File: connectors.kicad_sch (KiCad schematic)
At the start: 11 parts, among them J4 USB_C_pycubed, J5 1985807, J6 35362-0650, J7 1985807, J8 1985807, J9 1985807

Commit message: schematic update
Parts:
- removed C32: 4.7uF, Capacitor_SMD:C_0603_1608Metric, symbol Device:C_Small
- removed C33: 0.1uF, Capacitor_SMD:C_0603_1608Metric, symbol Device:C_Small
- removed C34: 22uF, Capacitor_SMD:C_0603_1608Metric, symbol Device:C_Small
- removed J4: USB_C_pycubed, mainboard:USB_C_Receptacle_XKB_U262-161N-4BVC11, symbol mainboard:USB_C_pycubed
- removed J5, J7, J8, J9: 1985807, mainboard:SCREWTERMINAL-3.5MM-2_LOCK, symbol mainboard:M023.5MM_LOCK
- removed J6: 35362-0650, mainboard:MOLEX_35362-0650, symbol mainboard:35362-0650
- removed R39, R40: 5.1k, Resistor_SMD:R_0603_1608Metric, symbol Device:R_US
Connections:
- no-connect marks 2 -> 0
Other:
- note removed: "(Screw Terminals)"
- note removed: "Battery Board"
- note removed: "Battery Connection"
- note removed: "High Side Switches (Screw Terminals)"
- note removed: "Low Side Switch"
- note removed: "Power Connectors: USB-C Power Delivery to 2S Li-ion Battery"

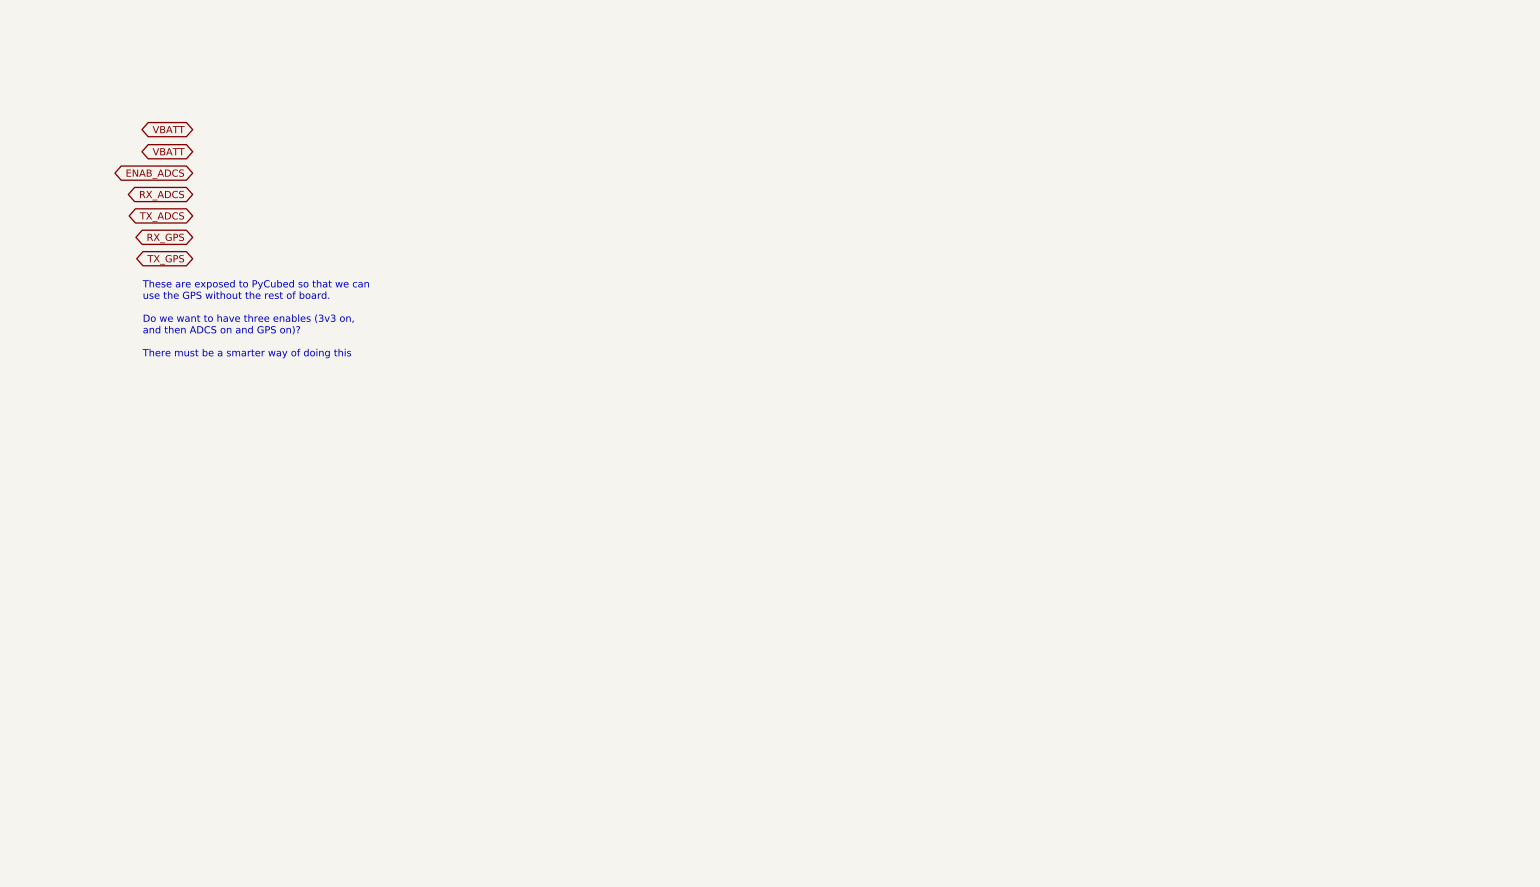
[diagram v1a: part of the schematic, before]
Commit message: update schematic
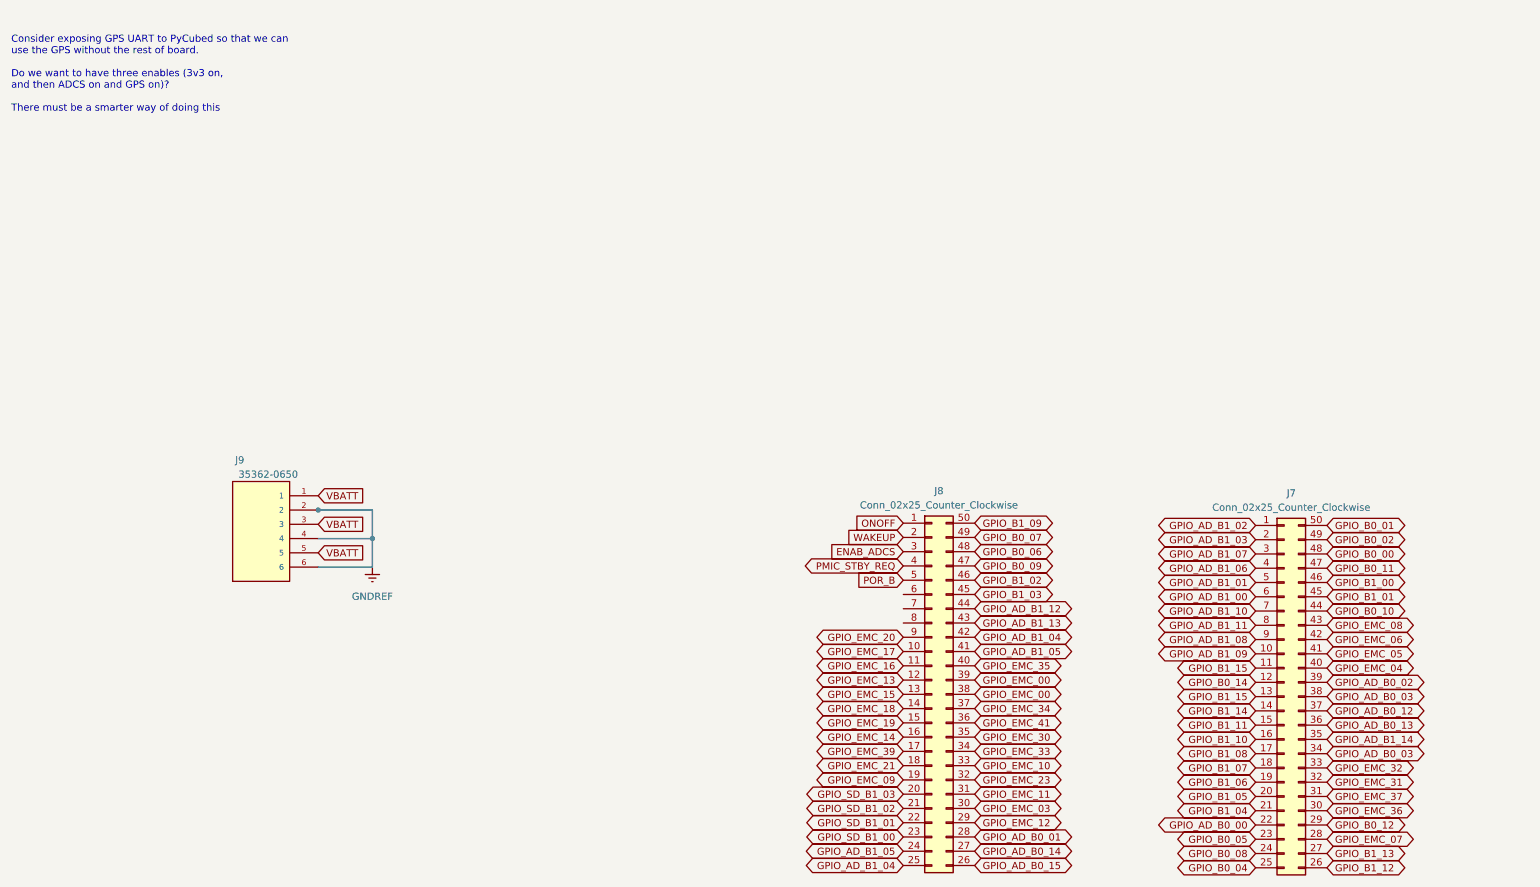
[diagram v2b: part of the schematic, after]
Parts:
- added J7, J8: Conn_02x25_Counter_Clockwise, symbol Connector_Generic:Conn_02x25_Counter_Clockwise
- added J9: 35362-0650, mainboard:MOLEX_35362-0650, symbol mainboard:35362-0650
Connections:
- net ENAB_ADCS: now also J8.3 (Pin_3)
- net VBATT: now also J9.1, J9.3, J9.5
- new net: J9.2, J9.4, J9.6
- new net GPIO_AD_B0_00: J7.22 (Pin_22)
- new net GPIO_AD_B0_01: J8.28 (Pin_28)
- new net GPIO_AD_B0_02: J7.39 (Pin_39)
- new net GPIO_AD_B0_03: J7.34 (Pin_34), J7.38 (Pin_38)
- new net GPIO_AD_B0_12: J7.37 (Pin_37)
- new net GPIO_AD_B0_13: J7.36 (Pin_36)
- new net GPIO_AD_B0_14: J8.27 (Pin_27)
- new net GPIO_AD_B0_15: J8.26 (Pin_26)
- new net GPIO_AD_B1_00: J7.6 (Pin_6)
- new net GPIO_AD_B1_01: J7.5 (Pin_5)
- new net GPIO_AD_B1_02: J7.1 (Pin_1)
- new net GPIO_AD_B1_03: J7.2 (Pin_2)
- new net GPIO_AD_B1_04: J8.25 (Pin_25), J8.42 (Pin_42)
- new net GPIO_AD_B1_05: J8.24 (Pin_24), J8.41 (Pin_41)
- new net GPIO_AD_B1_06: J7.4 (Pin_4)
- new net GPIO_AD_B1_07: J7.3 (Pin_3)
- new net GPIO_AD_B1_08: J7.9 (Pin_9)
- new net GPIO_AD_B1_09: J7.10 (Pin_10)
- new net GPIO_AD_B1_10: J7.7 (Pin_7)
- new net GPIO_AD_B1_11: J7.8 (Pin_8)
- new net GPIO_AD_B1_12: J8.44 (Pin_44)
- new net GPIO_AD_B1_13: J8.43 (Pin_43)
- new net GPIO_AD_B1_14: J7.35 (Pin_35)
- new net GPIO_B0_00: J7.48 (Pin_48)
- new net GPIO_B0_01: J7.50 (Pin_50)
- new net GPIO_B0_02: J7.49 (Pin_49)
- new net GPIO_B0_04: J7.25 (Pin_25)
- new net GPIO_B0_05: J7.23 (Pin_23)
- new net GPIO_B0_06: J8.48 (Pin_48)
- new net GPIO_B0_07: J8.49 (Pin_49)
- new net GPIO_B0_08: J7.24 (Pin_24)
- new net GPIO_B0_09: J8.47 (Pin_47)
- new net GPIO_B0_10: J7.44 (Pin_44)
- new net GPIO_B0_11: J7.47 (Pin_47)
- new net GPIO_B0_12: J7.29 (Pin_29)
- new net GPIO_B0_14: J7.12 (Pin_12)
- new net GPIO_B1_00: J7.46 (Pin_46)
- new net GPIO_B1_01: J7.45 (Pin_45)
- new net GPIO_B1_02: J8.46 (Pin_46)
- new net GPIO_B1_03: J8.45 (Pin_45)
- new net GPIO_B1_04: J7.21 (Pin_21)
- new net GPIO_B1_05: J7.20 (Pin_20)
- new net GPIO_B1_06: J7.19 (Pin_19)
- new net GPIO_B1_07: J7.18 (Pin_18)
- new net GPIO_B1_08: J7.17 (Pin_17)
- new net GPIO_B1_09: J8.50 (Pin_50)
- new net GPIO_B1_10: J7.16 (Pin_16)
- new net GPIO_B1_11: J7.15 (Pin_15)
- new net GPIO_B1_12: J7.26 (Pin_26)
- new net GPIO_B1_13: J7.27 (Pin_27)
- new net GPIO_B1_14: J7.14 (Pin_14)
- new net GPIO_B1_15: J7.11 (Pin_11), J7.13 (Pin_13)
- new net GPIO_EMC_00: J8.38 (Pin_38), J8.39 (Pin_39)
- new net GPIO_EMC_03: J8.30 (Pin_30)
- new net GPIO_EMC_04: J7.40 (Pin_40)
- new net GPIO_EMC_05: J7.41 (Pin_41)
- new net GPIO_EMC_06: J7.42 (Pin_42)
- new net GPIO_EMC_07: J7.28 (Pin_28)
- new net GPIO_EMC_08: J7.43 (Pin_43)
- new net GPIO_EMC_09: J8.19 (Pin_19)
- new net GPIO_EMC_10: J8.33 (Pin_33)
- new net GPIO_EMC_11: J8.31 (Pin_31)
- new net GPIO_EMC_12: J8.29 (Pin_29)
- new net GPIO_EMC_13: J8.12 (Pin_12)
- new net GPIO_EMC_14: J8.16 (Pin_16)
- new net GPIO_EMC_15: J8.13 (Pin_13)
- new net GPIO_EMC_16: J8.11 (Pin_11)
- new net GPIO_EMC_17: J8.10 (Pin_10)
- new net GPIO_EMC_18: J8.14 (Pin_14)
- new net GPIO_EMC_19: J8.15 (Pin_15)
- new net GPIO_EMC_20: J8.9 (Pin_9)
- new net GPIO_EMC_21: J8.18 (Pin_18)
- new net GPIO_EMC_23: J8.32 (Pin_32)
- new net GPIO_EMC_30: J8.35 (Pin_35)
- new net GPIO_EMC_31: J7.32 (Pin_32)
- new net GPIO_EMC_32: J7.33 (Pin_33)
- new net GPIO_EMC_33: J8.34 (Pin_34)
- new net GPIO_EMC_34: J8.37 (Pin_37)
- new net GPIO_EMC_35: J8.40 (Pin_40)
- new net GPIO_EMC_36: J7.30 (Pin_30)
- new net GPIO_EMC_37: J7.31 (Pin_31)
- new net GPIO_EMC_39: J8.17 (Pin_17)
- new net GPIO_EMC_41: J8.36 (Pin_36)
- new net GPIO_SD_B1_00: J8.23 (Pin_23)
- new net GPIO_SD_B1_01: J8.22 (Pin_22)
- new net GPIO_SD_B1_02: J8.21 (Pin_21)
- new net GPIO_SD_B1_03: J8.20 (Pin_20)
- new net ONOFF: J8.1 (Pin_1)
- new net PMIC_STBY_REQ: J8.4 (Pin_4)
- new net POR_B: J8.5 (Pin_5)
- new net WAKEUP: J8.2 (Pin_2)
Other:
- note added: "Consider exposing GPS UART to PyCubed so that we can use the GPS without the rest of board. Do we want to have three enables (3v3 on, and then ADCS on and GPS on)? There must be a smarter way of doing this"
- note removed: "These are exposed to PyCubed so that we can use the GPS without the rest of board. Do we want to have three enables (3v3 on, and then ADCS on and GPS on)? There must be a smarter way of doing this"

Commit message: hmm
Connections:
- net ENAB_ADCS: now also J8.6 (Pin_6)
- net RX_GPS: now reaches J8.7 (Pin_7)
- net TX_GPS: now reaches J8.8 (Pin_8)
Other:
- moved on the sheet: J9
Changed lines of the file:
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@@
 (kicad_sch (version 20230121) (generator eeschema)
   (paper "USLedger")
-  (junction (at 80.264 109.5248) (diameter 0) (color 0 0 0 0)
-  )
-  (junction (at 70.612 104.4448) (diameter 0) (color 0 0 0 0)
+  (junction (at 93.0148 115.7224) (diameter 0) (color 0 0 0 0)
+  )
+  (junction (at 83.3628 110.6424) (diameter 0) (color 0 0 0 0)
   )
   (bus_entry (at 407.67 18.161) (size -2.54 2.54)
@@
     (stroke (width 0) (type default))
   )
-  (wire (pts (xy 80.264 114.6048) (xy 70.612 114.6048))
-    (stroke (width 0) (type default))
-  )
-  (wire (pts (xy 70.612 104.4448) (xy 80.264 104.4448))
-    (stroke (width 0) (type default))
-  )
-  (wire (pts (xy 80.264 109.5248) (xy 80.264 114.6048))
+  (wire (pts (xy 93.0148 120.8024) (xy 83.3628 120.8024))
+    (stroke (width 0) (type default))
+  )
+  (wire (pts (xy 83.3628 110.6424) (xy 93.0148 110.6424))
+    (stroke (width 0) (type default))
+  )
+  (wire (pts (xy 93.0148 115.7224) (xy 93.0148 120.8024))
     (stroke (width 0) (type default))
   )
@@
     (stroke (width 0) (type default))
   )
-  (wire (pts (xy 80.264 109.5248) (xy 70.612 109.5248))
+  (wire (pts (xy 93.0148 115.7224) (xy 83.3628 115.7224))
     (stroke (width 0) (type default))
   )
@@
     (stroke (width 0) (type default))
   )
-  (wire (pts (xy 70.5612 104.4448) (xy 70.612 104.4448))
+  (wire (pts (xy 83.312 110.6424) (xy 83.3628 110.6424))
     (stroke (width 0) (type default))
   )
@@
     (stroke (width 0) (type default))
   )
-  (wire (pts (xy 80.264 104.4448) (xy 80.264 109.5248))
+  (wire (pts (xy 93.0148 110.6424) (xy 93.0148 115.7224))
     (stroke (width 0) (type default))
   )
@@
     (effects (font (size 1.27 1.27)) (justify left bottom))
   )
-  (global_label "VBATT" (shape input) (at 70.612 106.9848 0) (fields_autoplaced)
-    (effects (font (size 1.27 1.27)) (justify left))
-    (property "Intersheetrefs" "${INTERSHEET_REFS}" (at 78.9796 106.9848 0)
+  (global_label "VBATT" (shape input) (at 83.3628 113.1824 0) (fields_autoplaced)
+    (effects (font (size 1.27 1.27)) (justify left))
+    (property "Intersheetrefs" "${INTERSHEET_REFS}" (at 91.7304 113.1824 0)
       (effects (font (size 1.27 1.27)) (justify left) hide)
     )
@@
     )
   )
+  (global_label "RX_GPS" (shape bidirectional) (at 174.8028 122.0216 180) (fields_autoplaced)
+    (effects (font (size 1.27 1.27)) (justify right))
+    (property "Intersheetrefs" "${INTERSHEET_REFS}" (at 163.5097 122.0216 0)
+      (effects (font (size 1.27 1.27)) (justify right) hide)
+    )
+  )
   (global_label "GPIO_AD_B1_12" (shape bidirectional) (at 187.5028 122.0216 0) (fields_autoplaced)
     (effects (font (size 1.27 1.27)) (justify left))
@@
     )
   )
+  (global_label "ENAB_ADCS" (shape bidirectional) (at 174.8028 119.4816 180) (fields_autoplaced)
+    (effects (font (size 1.27 1.27)) (justify right))
+    (property "Intersheetrefs" "${INTERSHEET_REFS}" (at 160.0625 119.4816 0)
+      (effects (font (size 1.27 1.27)) (justify right) hide)
+    )
+  )
   (global_label "GPIO_EMC_35" (shape bidirectional) (at 187.5028 132.1816 0) (fields_autoplaced)
     (effects (font (size 1.27 1.27)) (justify left))
@@
     )
   )
+  (global_label "TX_GPS" (shape bidirectional) (at 174.8028 124.5616 180) (fields_autoplaced)
+    (effects (font (size 1.27 1.27)) (justify right))
+    (property "Intersheetrefs" "${INTERSHEET_REFS}" (at 163.8121 124.5616 0)
+      (effects (font (size 1.27 1.27)) (justify right) hide)
+    )
+  )
   (global_label "GPIO_B1_05" (shape bidirectional) (at 237.5408 155.448 180) (fields_autoplaced)
     (effects (font (size 1.27 1.27)) (justify right))
@@
     )
   )
-  (global_label "VBATT" (shape input) (at 70.612 112.0648 0) (fields_autoplaced)
-    (effects (font (size 1.27 1.27)) (justify left))
-    (property "Intersheetrefs" "${INTERSHEET_REFS}" (at 78.9796 112.0648 0)
+  (global_label "VBATT" (shape input) (at 83.3628 118.2624 0) (fields_autoplaced)
+    (effects (font (size 1.27 1.27)) (justify left))
+    (property "Intersheetrefs" "${INTERSHEET_REFS}" (at 91.7304 118.2624 0)
       (effects (font (size 1.27 1.27)) (justify left) hide)
     )
@@
     )
   )
-  (global_label "VBATT" (shape input) (at 70.612 101.9048 0) (fields_autoplaced)
-    (effects (font (size 1.27 1.27)) (justify left))
-    (property "Intersheetrefs" "${INTERSHEET_REFS}" (at 78.9796 101.9048 0)
+  (global_label "VBATT" (shape input) (at 83.3628 108.1024 0) (fields_autoplaced)
+    (effects (font (size 1.27 1.27)) (justify left))
+    (property "Intersheetrefs" "${INTERSHEET_REFS}" (at 91.7304 108.1024 0)
       (effects (font (size 1.27 1.27)) (justify left) hide)
     )
@@
     )
   )
-  (symbol (lib_id "mainboard:35362-0650") (at 60.452 109.5248 0) (unit 1)
+  (symbol (lib_id "mainboard:35362-0650") (at 73.2028 115.7224 0) (unit 1)
     (in_bom yes) (on_board yes) (dnp no)
-    (property "Reference" "J9" (at 56.642 95.5548 0)
+    (property "Reference" "J9" (at 69.3928 101.7524 0)
       (effects (font (size 1.27 1.27)))
     )
-    (property "Value" "35362-0650" (at 61.722 98.0948 0)
+    (property "Value" "35362-0650" (at 74.4728 104.2924 0)
       (effects (font (size 1.27 1.27)))
     )
-    (property "Footprint" "mainboard:MOLEX_35362-0650" (at 54.102 118.4148 90)
+    (property "Footprint" "mainboard:MOLEX_35362-0650" (at 66.8528 124.6124 90)
       (effects (font (size 1.27 1.27)) (justify left bottom) hide)
     )
-    (property "Datasheet" "" (at 60.452 109.5248 0)
+    (property "Datasheet" "" (at 73.2028 115.7224 0)
       (effects (font (size 1.27 1.27)) (justify left bottom) hide)
     )
@@
     )
   )
-  (symbol (lib_name "GNDREF_1") (lib_id "power:GNDREF") (at 80.264 114.6556 0) (unit 1)
+  (symbol (lib_name "GNDREF_1") (lib_id "power:GNDREF") (at 93.0148 120.8532 0) (unit 1)
     (in_bom yes) (on_board yes) (dnp no) (fields_autoplaced)
-    (property "Reference" "#PWR033" (at 80.264 121.0056 0)
+    (property "Reference" "#PWR033" (at 93.0148 127.2032 0)
       (effects (font (size 1.27 1.27)) hide)
     )
-    (property "Value" "GNDREF" (at 80.264 119.8372 0)
+    (property "Value" "GNDREF" (at 93.0148 126.0348 0)
       (effects (font (size 1.27 1.27)))
     )
-    (property "Footprint" "" (at 80.264 114.6556 0)
+    (property "Footprint" "" (at 93.0148 120.8532 0)
       (effects (font (size 1.27 1.27)) hide)
     )
-    (property "Datasheet" "" (at 80.264 114.6556 0)
+    (property "Datasheet" "" (at 93.0148 120.8532 0)
       (effects (font (size 1.27 1.27)) hide)
     )
